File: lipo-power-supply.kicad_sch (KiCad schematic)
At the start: 19 parts, among them J3 Conn_01x02_Female, U10 STC3100IQT, U4 MIC5528, U5 MCP1726

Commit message: added test point for VDD_EXT
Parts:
- added TP4: VDD_EXT, TestPoint:TestPoint_Pad_D1.5mm, symbol Connector:TestPoint
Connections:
- new net VDD_EXT: TP4.1
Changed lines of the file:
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@@
+    (stroke (width 0) (type default) (color 0 0 0 0))
+  )
+  (wire (pts (xy 254 15.24) (xy 259.08 15.24))
     (stroke (width 0) (type default) (color 0 0 0 0))
   )
@@
     (effects (font (size 1.27 1.27)) (justify right))
     (property "Intersheet References" "${INTERSHEET_REFS}" (id 0) (at 36.2917 82.4706 0)
+      (effects (font (size 1.27 1.27)) (justify right) hide)
+    )
+  )
+  (global_label "VDD_EXT" (shape input) (at 254 15.24 180) (fields_autoplaced)
+    (effects (font (size 1.27 1.27)) (justify right))
+    (property "Intersheet References" "${INTERSHEET_REFS}" (id 0) (at 243.6645 15.1606 0)
       (effects (font (size 1.27 1.27)) (justify right) hide)
     )
@@
       (effects (font (size 1.27 1.27)) hide)
     )
+    (pin "1")
+  )
+  (symbol (lib_id "Connector:TestPoint") (at 259.08 15.24 270) (unit 1)
+    (in_bom yes) (on_board yes)
+    (property "Reference" "TP4" (id 0) (at 267.4422 13.7745 90)
+      (effects (font (size 1.27 1.27)) (justify right))
+    )
+    (property "Value" "VDD_EXT" (id 1) (at 272.0413 15.982 90)
+      (effects (font (size 1.27 1.27)) (justify right))
+    )
+    (property "Footprint" "TestPoint:TestPoint_Pad_D1.5mm" (id 2) (at 259.08 20.32 0)
+      (effects (font (size 1.27 1.27)) hide)
+    )
+    (property "Datasheet" "~" (id 3) (at 259.08 20.32 0)
+      (effects (font (size 1.27 1.27)) hide)
+    )

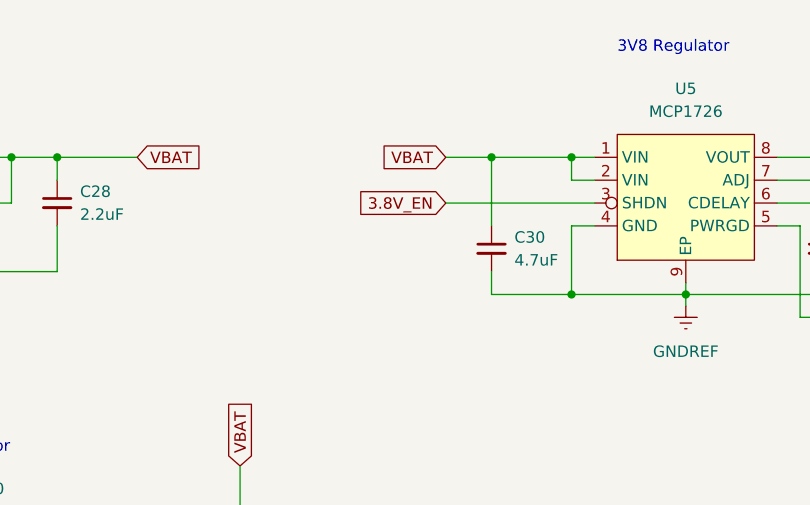
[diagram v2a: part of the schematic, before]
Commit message: 3.8V LDO: added output enable control from uc
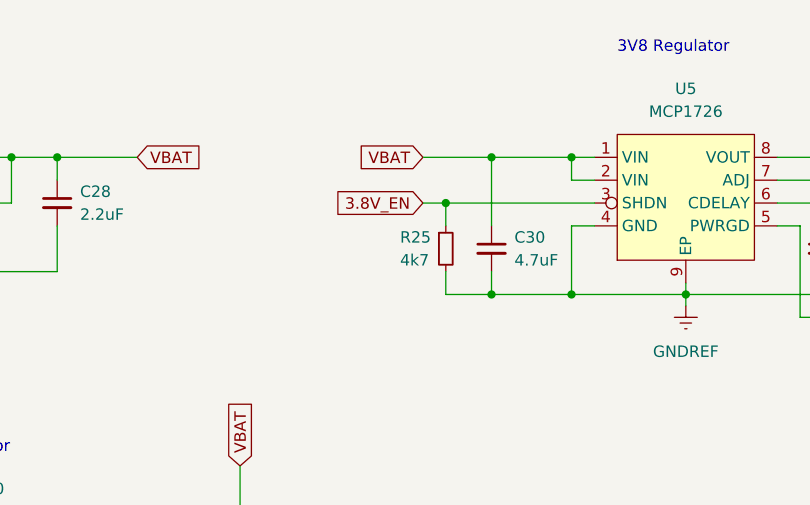
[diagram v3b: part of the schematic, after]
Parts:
- added R25: 4k7, Resistor_SMD:R_0402_1005Metric, symbol Device:R_Small
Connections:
- net 3.8V_EN: now also R25.1
- net GNDREF: now also R25.2
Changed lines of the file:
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@@
   (junction (at 74.93 27.94) (diameter 0) (color 0 0 0 0)
   )
+  (junction (at 123.19 33.02) (diameter 0) (color 0 0 0 0)
+  )
   (junction (at 201.93 21.59) (diameter 0) (color 0 0 0 0)
   )
+  (junction (at 128.27 43.18) (diameter 0) (color 0 0 0 0)
+  )
   (junction (at 62.23 40.64) (diameter 0) (color 0 0 0 0)
   )
@@
     (stroke (width 0) (type default) (color 0 0 0 0))
   )
-  (wire (pts (xy 123.19 27.94) (xy 128.27 27.94))
+  (wire (pts (xy 120.65 27.94) (xy 128.27 27.94))
     (stroke (width 0) (type default) (color 0 0 0 0))
   )
@@
     (stroke (width 0) (type default) (color 0 0 0 0))
   )
+  (wire (pts (xy 123.19 40.64) (xy 123.19 43.18))
+    (stroke (width 0) (type default) (color 0 0 0 0))
+  )
   (wire (pts (xy 52.07 33.02) (xy 52.07 40.64))
     (stroke (width 0) (type default) (color 0 0 0 0))
@@
     (stroke (width 0) (type default) (color 0 0 0 0))
   )
+  (wire (pts (xy 123.19 43.18) (xy 128.27 43.18))
+    (stroke (width 0) (type default) (color 0 0 0 0))
+  )
   (wire (pts (xy 256.54 35.56) (xy 256.54 40.64))
     (stroke (width 0) (type default) (color 0 0 0 0))
   )
+  (wire (pts (xy 123.19 33.02) (xy 139.7 33.02))
+    (stroke (width 0) (type default) (color 0 0 0 0))
+  )
   (wire (pts (xy 176.53 29.21) (xy 176.53 30.48))
     (stroke (width 0) (type default) (color 0 0 0 0))
@@
     (stroke (width 0) (type default) (color 0 0 0 0))
   )
+  (wire (pts (xy 123.19 33.02) (xy 123.19 35.56))
+    (stroke (width 0) (type default) (color 0 0 0 0))
+  )
   (wire (pts (xy 248.92 35.56) (xy 248.92 40.64))
     (stroke (width 0) (type default) (color 0 0 0 0))
@@
     (stroke (width 0) (type default) (color 0 0 0 0))
   )
-  (wire (pts (xy 123.19 33.02) (xy 139.7 33.02))
+  (wire (pts (xy 120.65 33.02) (xy 123.19 33.02))
     (stroke (width 0) (type default) (color 0 0 0 0))
   )
@@
     (effects (font (size 1.27 1.27)) (justify left bottom))
   )
-  (global_label "3.8V_EN" (shape input) (at 123.19 33.02 180) (fields_autoplaced)
+  (global_label "3.8V_EN" (shape input) (at 120.65 33.02 180) (fields_autoplaced)
     (effects (font (size 1.27 1.27)) (justify right))
-    (property "Intersheet References" "${INTERSHEET_REFS}" (id 0) (at 113.2174 33.0994 0)
+    (property "Intersheet References" "${INTERSHEET_REFS}" (id 0) (at 110.6774 33.0994 0)
       (effects (font (size 1.27 1.27)) (justify right) hide)
     )
@@
     )
   )
-  (global_label "VBAT" (shape input) (at 123.19 27.94 180) (fields_autoplaced)
+  (global_label "VBAT" (shape input) (at 120.65 27.94 180) (fields_autoplaced)
     (effects (font (size 1.27 1.27)) (justify right))
-    (property "Intersheet References" "${INTERSHEET_REFS}" (id 0) (at 116.3621 28.0194 0)
+    (property "Intersheet References" "${INTERSHEET_REFS}" (id 0) (at 113.8221 28.0194 0)
       (effects (font (size 1.27 1.27)) (justify right) hide)
     )
@@
     (pin "1")
   )
+  (symbol (lib_id "Device:R_Small") (at 123.19 38.1 0) (unit 1)
+    (in_bom yes) (on_board yes)
+    (property "Reference" "R25" (id 0) (at 118.11 36.83 0)
+      (effects (font (size 1.27 1.27)) (justify left))
+    )
+    (property "Value" "4k7" (id 1) (at 118.11 39.37 0)
+      (effects (font (size 1.27 1.27)) (justify left))
+    )
+    (property "Footprint" "Resistor_SMD:R_0402_1005Metric" (id 2) (at 123.19 38.1 0)
+      (effects (font (size 1.27 1.27)) hide)
+    )
+    (property "Datasheet" "~" (id 3) (at 123.19 38.1 0)
+      (effects (font (size 1.27 1.27)) hide)
+    )
+    (pin "1")
+    (pin "2")
+  )
   (symbol (lib_id "Device:C_Small") (at 128.27 38.1 0) (unit 1)

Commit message: updated footprints and PCB
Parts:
- C32: footprint Capacitor_SMD:C_0603_1608Metric -> Capacitor_SMD:C_0201_0603Metric
- C34: value 1uF -> 10uF
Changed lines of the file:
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@@
       (effects (font (size 1.27 1.27)) (justify left))
     )
-    (property "Footprint" "Capacitor_SMD:C_0603_1608Metric" (id 2) (at 165.1 38.1 0)
+    (property "Footprint" "Capacitor_SMD:C_0201_0603Metric" (id 2) (at 165.1 38.1 0)
       (effects (font (size 1.27 1.27)) hide)
     )
@@
       (effects (font (size 1.27 1.27)) (justify left))
     )
-    (property "Value" "1uF" (id 1) (at 204.47 31.7562 0)
-      (effects (font (size 1.27 1.27)) (justify left))
-    )
+    (property "Value" "10uF" (id 1) (at 204.47 31.7562 0)
+      (effects (font (size 1.27 1.27)) (justify left))
+    )

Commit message: ok before switching to EG91EX footprint
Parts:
- C32: footprint Capacitor_SMD:C_0201_0603Metric -> Capacitor_SMD:C_0402_1005Metric
- R10, R13: footprint Resistor_SMD:R_0402_1005Metric -> Resistor_SMD:R_0603_1608Metric
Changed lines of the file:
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@@
       (effects (font (size 1.27 1.27)) (justify left))
     )
-    (property "Footprint" "Capacitor_SMD:C_0201_0603Metric" (id 2) (at 165.1 38.1 0)
+    (property "Footprint" "Capacitor_SMD:C_0402_1005Metric" (id 2) (at 165.1 38.1 0)
       (effects (font (size 1.27 1.27)) hide)
     )
@@
       (effects (font (size 1.27 1.27)) (justify left))
     )
-    (property "Footprint" "Resistor_SMD:R_0402_1005Metric" (id 2) (at 30.48 87.63 0)
+    (property "Footprint" "Resistor_SMD:R_0603_1608Metric" (id 2) (at 30.48 87.63 0)
       (effects (font (size 1.27 1.27)) hide)
     )
@@
       (effects (font (size 1.27 1.27)) (justify left))
     )
-    (property "Footprint" "Resistor_SMD:R_0402_1005Metric" (id 2) (at 176.53 26.67 0)
-      (effects (font (size 1.27 1.27)) hide)
-    )
+    (property "Footprint" "Resistor_SMD:R_0603_1608Metric" (id 2) (at 176.53 26.67 0)
+      (effects (font (size 1.27 1.27)) hide)
+    )
